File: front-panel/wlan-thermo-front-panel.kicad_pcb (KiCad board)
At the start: 2 copper layers, 57 x 43.5 mm, 29 parts, among them IC1 ME6211C33M5G-N, J1 PROG_HDR, J2 Conn_01x02, J3 Conn_01x02, Q1 SS8050-G, Q2 SS8050-G, SW1 SW_Push, SW2 RotaryEncoder_Switch, U1 ESP-12F, U2 SHT4x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

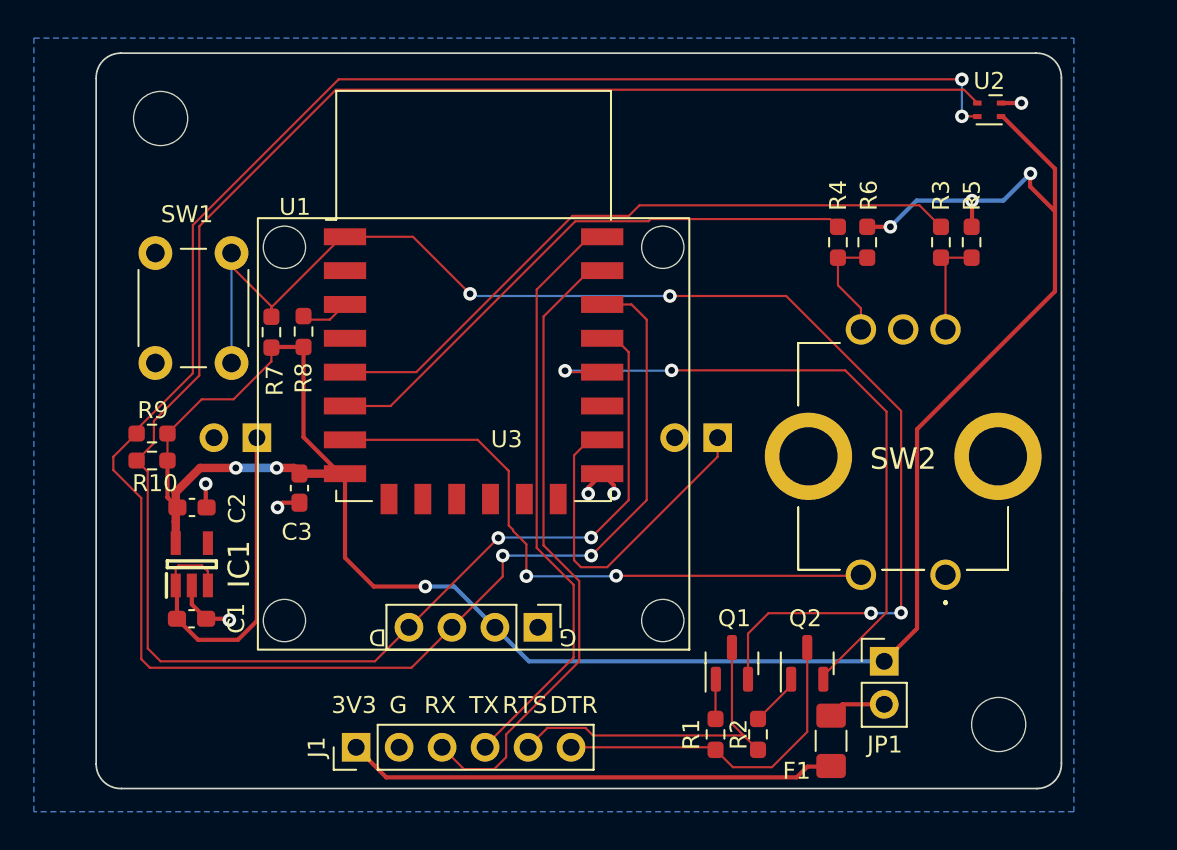
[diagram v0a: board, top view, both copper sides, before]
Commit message: Corrected traces and spacings for assembly
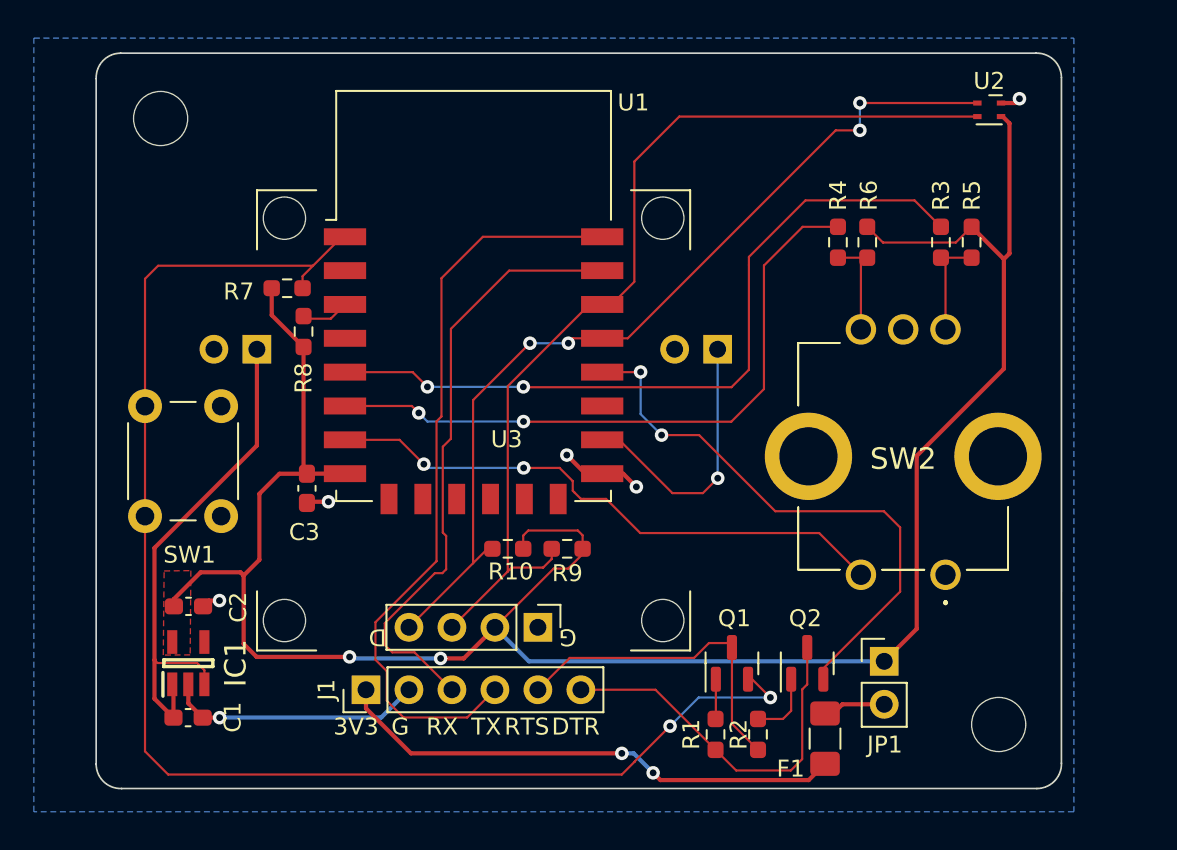
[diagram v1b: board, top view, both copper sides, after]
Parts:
- moved R9 25.5 mm to (124.2, 65.7)
- moved R10 21.7 mm to (120.7, 65.7)
- moved SW1 16.4 mm to (99.3, 63.8), turned to 90 degrees
- moved C2 5.85 mm to (101.9, 69.1)
- moved C1 5.85 mm to (101.8, 75.7)
- moved IC1 5.85 mm to (101.8, 72.5)
- moved J2 5.23 mm to (105.9, 53.9)
- moved J3 5.23 mm to (133.1, 53.9)
- moved J1 3.45 mm to (112.3, 74.1)
- moved R7 2.76 mm to (107.7, 50.3), turned to 0 degrees
- moved C3 0.44 mm to (108.8, 62.2)
- moved F1 0.38 mm to (139.5, 77.0)
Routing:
- net GPIO5_SCL: track 129.0 -> 57.6 mm, vias 4 -> 0
- net GPIO4_SDA: track 119.7 -> 54.5 mm, vias 2 -> 4
- net GND: track 10.8 -> 23.7 mm
- net GPIO4_TX: track 35.3 -> 44.9 mm
- net +5V: track 22.5 -> 30.8 mm
- net ~{GPIO0}: track 39.6 -> 33.7 mm
- net GPIO14_RENCLK: track 39.8 -> 44.7 mm, vias 0 -> 2
- net GPIO12_RENDAT: track 33.9 -> 38.6 mm, vias 0 -> 2
- net GPIO15_RELAY: track 20.7 -> 16.1 mm, vias 0 -> 1
- net ~{RESET}: track 79.5 -> 83.5 mm, vias 4 -> 2
- net GPIO13_RENBTN: track 36.9 -> 34.1 mm
- net DTR: track 20.3 -> 22.1 mm
- net GPIO3_RX: track 37.9 -> 36.2 mm
- net /3v3PROG: track 29.1 -> 30.4 mm, vias 0 -> 2
- net RTS: track 20.3 -> 19.4 mm
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- added copper zone on F.Cu, net +3V3

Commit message: Fixed strapping pins for booting and loading
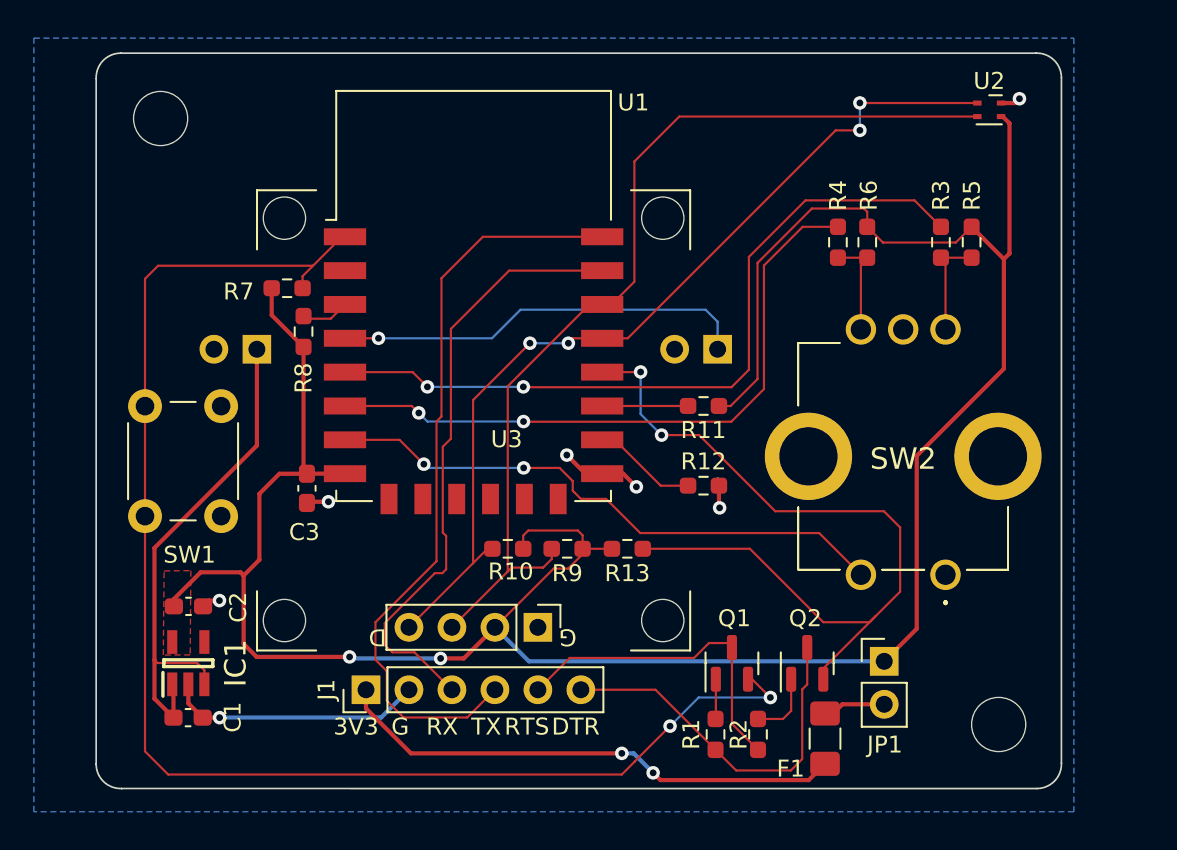
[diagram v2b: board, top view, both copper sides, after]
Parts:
- added R11: 10k, Resistor_SMD:R_0603_1608Metric_Pad0.98x0.95mm_HandSolder, F.Cu at (132.3, 57.3)
- added R12: 10k, Resistor_SMD:R_0603_1608Metric_Pad0.98x0.95mm_HandSolder, F.Cu at (132.3, 62.0)
- added R13: 10k, Resistor_SMD:R_0603_1608Metric_Pad0.98x0.95mm_HandSolder, F.Cu at (127.8, 65.7)
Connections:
- J3 pad 1: GPIO15_RELAY -> GPIO16_RELAY
- U1 pad 16: GPIO15_RELAY -> Net-(U1-GPIO15)
- U1 pad 17: unconnected-(U1-GPIO2-Pad17) -> Net-(U1-GPIO2)
- U1 pad 4: unconnected-(U1-GPIO16-Pad4) -> GPIO16_RELAY
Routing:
- net GPIO16_RELAY: track 0.00 -> 24.6 mm, vias 0 -> 1
- net +3V3: track 129.3 -> 149.6 mm
- net GPIO15_RELAY: track 16.1 -> 0.00 mm, vias 1 -> 0
- net ~{GPIO0}: track 33.7 -> 49.4 mm
- net Net-(U1-GPIO15): track 0.00 -> 6.20 mm
- net Net-(U1-GPIO2): track 0.00 -> 5.07 mm
- net GND: track 23.7 -> 25.0 mm, vias 6 -> 7
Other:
- board text added: "WLAN Thermostat Frontpanel v1.1 (2023)"
- board text removed: "WLAN Thermostat Frontpanel v1.0 (2023)"

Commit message: Decoupled sht40 from main ground plane
In order to measure the ambient temperature and not the board one
the following measures where taken:

- Remove the ground plane from the area around the sensor
- Turn all connections around so that a cut-out can be drawn around the component
- Expose the copper on the back of the sensor's ground plane as additional heat disipation
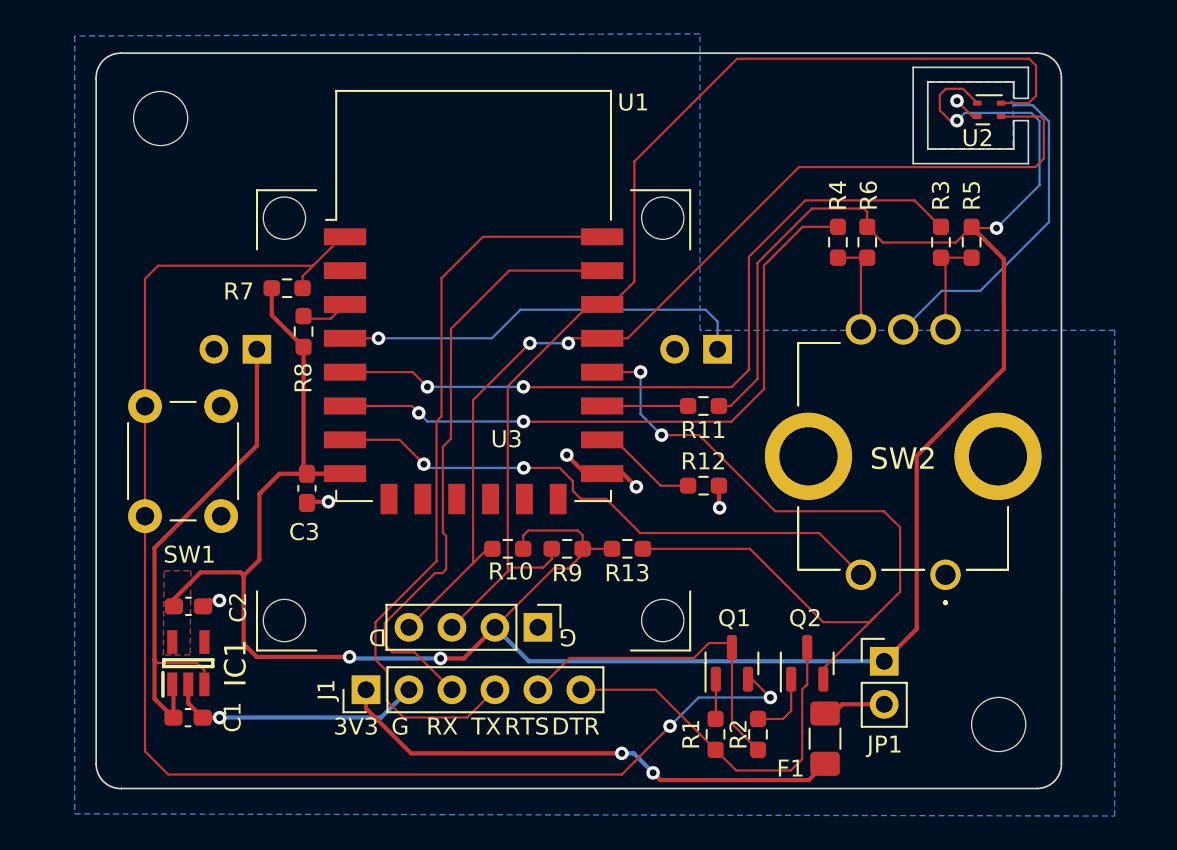
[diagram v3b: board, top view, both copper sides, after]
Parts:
- turned U2 to 180 degrees
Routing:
- net GND: track 25.0 -> 45.3 mm
- net +3V3: track 149.6 -> 159.9 mm, vias 2 -> 4
- net GPIO5_SCL: track 57.6 -> 66.7 mm
- net GPIO4_SDA: track 54.5 -> 61.0 mm, vias 4 -> 2
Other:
- outline, holes or cut-outs redrawn

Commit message: Changed strapping pins to resistor network
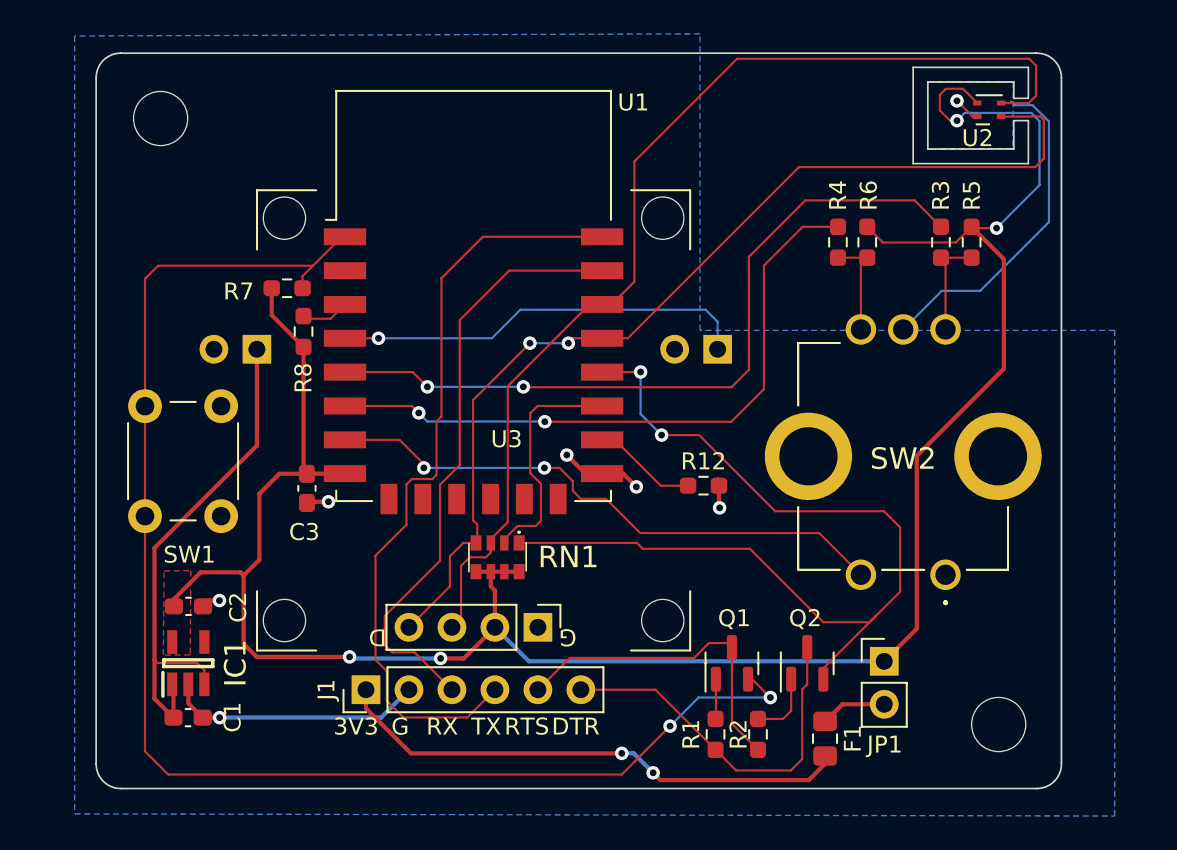
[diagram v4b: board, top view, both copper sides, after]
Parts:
- removed R10, R11, R13, R9: 10k, Resistor_SMD:R_0603_1608Metric_Pad0.98x0.95mm_HandSolder
- added RN1: 10k, Chof747 Footprints:YC164JR07220RL, F.Cu at (120.1, 66.2)
- F1: footprint Fuse:Fuse_1206_3216Metric_Pad1.42x1.75mm_HandSolder -> Fuse:Fuse_0805_2012Metric_Pad1.15x1.40mm_HandSolder
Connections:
- U1 pad 17: Net-(U1-GPIO2) -> GPIO2
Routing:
- net +3V3: track 159.9 -> 132.7 mm
- net GPIO2: track 0.00 -> 13.9 mm
- net ~{GPIO0}: track 49.4 -> 56.9 mm
- net Net-(U1-GPIO2): track 5.07 -> 0.00 mm
- net GPIO5_SCL: track 66.7 -> 63.8 mm
- net GPIO4_SDA: track 61.0 -> 60.2 mm
- net GPIO4_TX: track 44.9 -> 45.6 mm

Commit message: Use UMH3N chip for autorestart cycle
- Removed Q1/Q2 and the two 10k resistors and replace it with UMH3N for autoreset
- Changed footprint of fuse to 0804
- Reorganised board to be smaller to fit into casing of existing wall switch
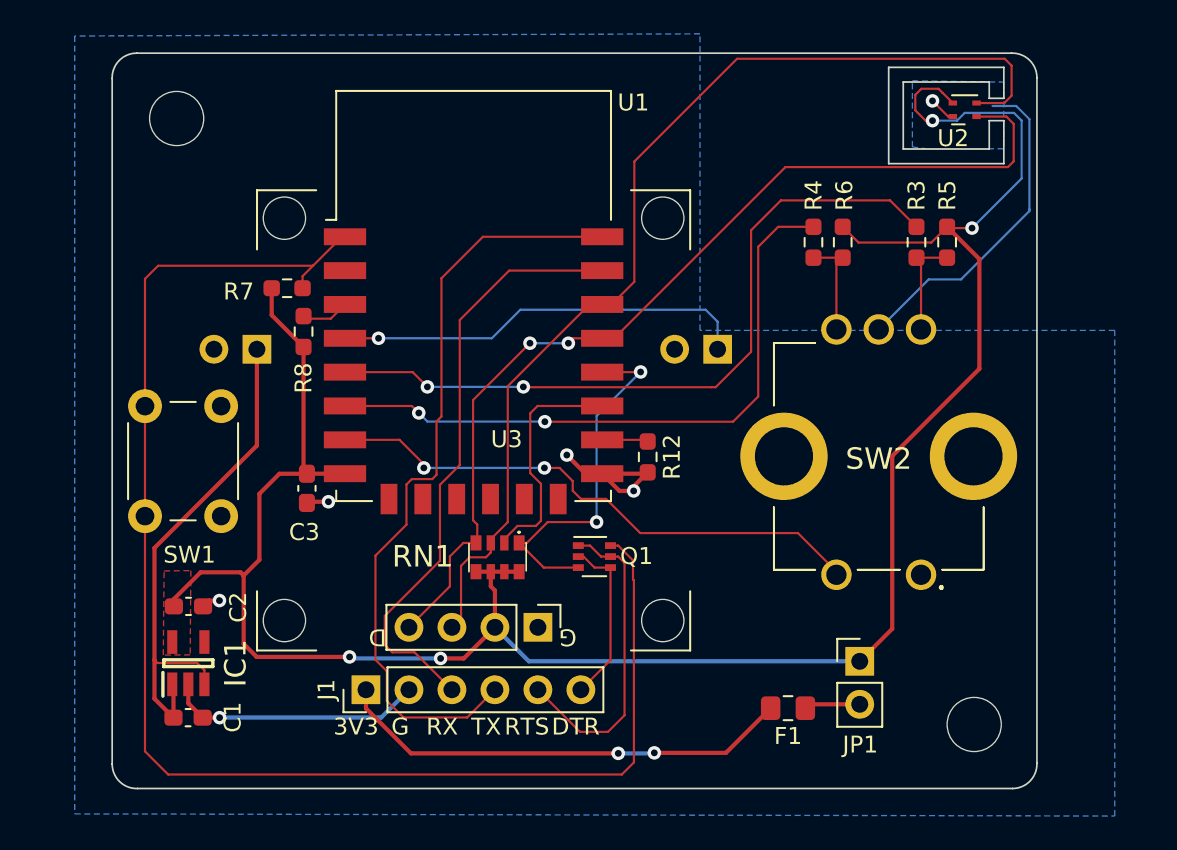
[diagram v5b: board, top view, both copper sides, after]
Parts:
- removed Q2: SS8050-G, Package_TO_SOT_SMD:SOT-23
- removed R1, R2: 10k, Resistor_SMD:R_0603_1608Metric_Pad0.98x0.95mm_HandSolder
- Q1: value SS8050-G -> UMH3N; footprint Package_TO_SOT_SMD:SOT-23 -> Package_TO_SOT_SMD:SOT-363_SC-70-6
- moved Q1 10.3 mm to (125.8, 66.2), turned to 0 degrees
- moved R12 3.71 mm to (129.0, 60.3), turned to -90 degrees
- moved F1 2.83 mm to (137.3, 75.2), turned to 180 degrees
- moved H2 1.45 mm to (148.3, 76.1)
- moved JP1 1.45 mm to (141.5, 72.4)
- moved R3 1.45 mm to (144.9, 47.6)
- moved R5 1.45 mm to (146.7, 47.6)
- moved R6 1.45 mm to (140.5, 47.6)
- moved SW2 1.45 mm to (145.1, 67.3)
- moved U2 1.45 mm to (147.7, 39.8)
- moved R4 1.45 mm to (138.8, 47.6)
- moved H1 0.95 mm to (101.2, 40.3)
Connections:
- Q1 pad 1: Net-(Q1-B) -> RTS
- Q1 pad 2: ~{RESET} -> DTR
- Q1 pad 3: RTS -> ~{GPIO0}
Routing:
- net ~{GPIO0}: track 56.9 -> 21.4 mm
- net DTR: track 22.1 -> 10.1 mm
- net Net-(Q2-B): track 4.02 -> 0.00 mm
- net Net-(U1-GPIO15): track 6.20 -> 2.73 mm
- net /3v3PROG: track 30.4 -> 27.2 mm
- net GND: track 45.3 -> 47.9 mm, vias 7 -> 6
- net Net-(Q1-B): track 2.36 -> 0.00 mm
- net ~{RESET}: track 83.5 -> 85.8 mm, vias 2 -> 0
- net GPIO4_SDA: track 60.2 -> 58.1 mm
- net GPIO5_SCL: track 63.8 -> 62.3 mm
- net GPIO13_RENBTN: track 34.3 -> 32.9 mm
- net GPIO14_RENCLK: track 44.7 -> 43.6 mm
- net +3V3: track 132.7 -> 131.8 mm
- net RTS: track 19.4 -> 18.7 mm
- net GPIO12_RENDAT: track 38.6 -> 38.0 mm
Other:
- board size 57 x 43.5 mm -> 54.7 x 43.5 mm

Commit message: Changed relay pin to avoid on on flash and boot
- Change relay pin to GPIO 13
- Change Rotary encoder pin to GPIO0 (also pulled up and provides extra feature: Rotary button works as flash button)
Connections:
- J3 pad 1: GPIO16_RELAY -> GPIO13_RELAY
- Q1 pad 3: ~{GPIO0} -> ~{GPIO0_RENBTN_FLASH}
- RN1 pad 1: ~{GPIO0} -> ~{GPIO0_RENBTN_FLASH}
- SW2 pad 2: GPIO13_RENBTN -> ~{GPIO0_RENBTN_FLASH}
- U1 pad 18: ~{GPIO0} -> ~{GPIO0_RENBTN_FLASH}
- U1 pad 4: GPIO16_RELAY -> unconnected-(U1-GPIO16-Pad4)
- U1 pad 7: GPIO13_RENBTN -> GPIO13_RELAY
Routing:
- net ~{GPIO0_RENBTN_FLASH}: track 0.00 -> 36.9 mm, vias 0 -> 2
- net GPIO13_RENBTN: track 32.9 -> 0.00 mm, vias 2 -> 0
- net GPIO13_RELAY: track 0.00 -> 28.5 mm, vias 0 -> 1
- net GPIO16_RELAY: track 24.6 -> 0.00 mm, vias 1 -> 0
- net ~{GPIO0}: track 21.4 -> 0.00 mm, vias 2 -> 0
